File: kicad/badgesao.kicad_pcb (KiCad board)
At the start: 6 copper layers, 38.1 x 50.8 mm, 267 parts, among them J1 Conn_01x03_Pin, J2 DEBUG, J3 USB_C_Receptacle_USB2.0_16P, Q1 Q_NPN_BEC, SW1 SW_Push, SW2 SW_Push, SW3 SW_Push, SW4 SW_Push, SW5 SW_Push, SW6 SW_Push, SW7 SW_Push, SW8 SW_Push, U1 XC6206P332MR, U2 ZD25WQ32CEIGR, U3 LSM6DS3, U4 TPS61022, U6 RP2040, X1 Simple_Addon_v2, Y1 12M

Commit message: connected buzzer and sel nets
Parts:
- J1: value Conn_01x03_Pin -> DISP_DBG
- LS1: value CMT-5023S-SMT-TR -> BUZZER
- Q1: value Q_NPN_BEC -> NPN_BEC
- SW1: value SW_Push -> UP
- SW2: value SW_Push -> DOWN
- SW3: value SW_Push -> LEFT
- SW4: value SW_Push -> RIGHT
- SW5: value SW_Push -> B
- SW6: value SW_Push -> A
- SW7: value SW_Push -> RESET
- SW8: value SW_Push -> BOOTSEL
- U1: value XC6206P332MR -> 3V3LDO
- U2: value ZD25WQ32CEIGR -> 32Mb QSPI
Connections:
- U6 pad 37: unconnected-(U6-GPIO25-Pad37) -> /BUZZER
- U6 pad 41: unconnected-(U6-GPIO29_ADC3-Pad41) -> /BOOTSEL

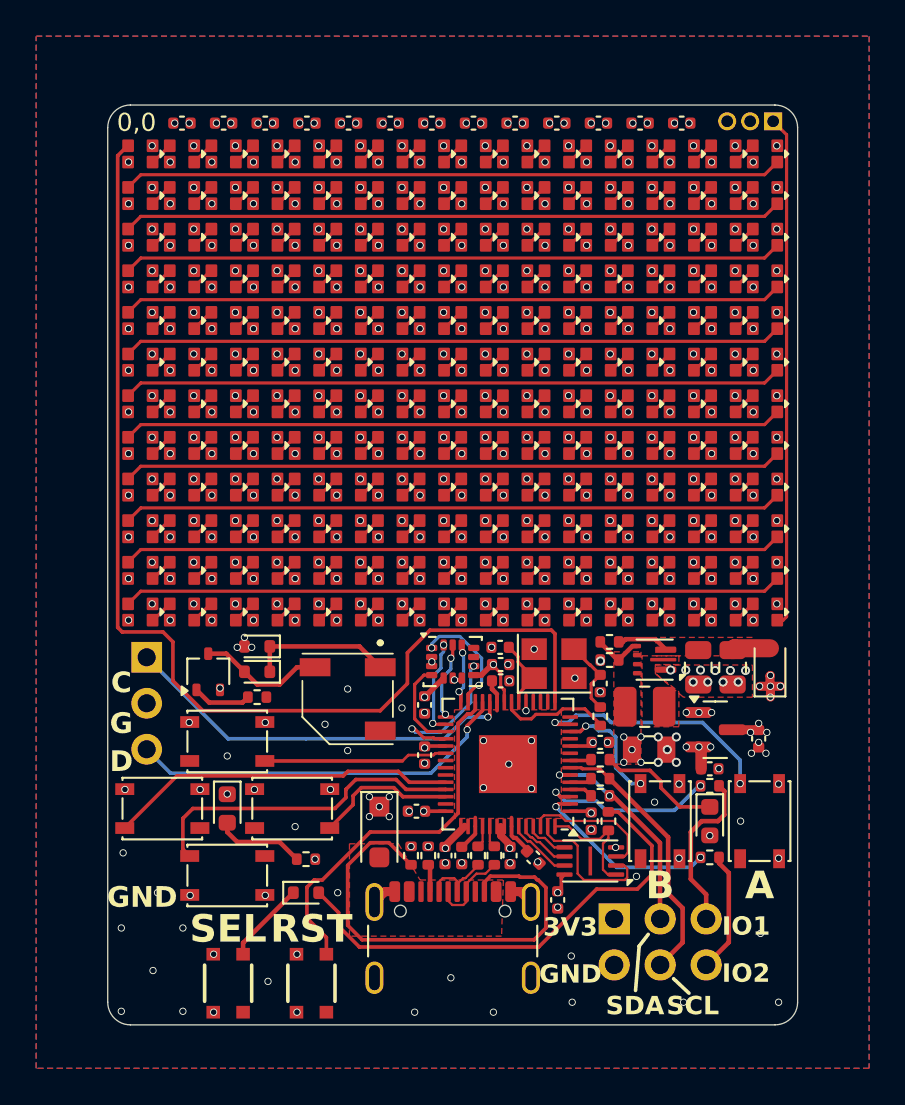
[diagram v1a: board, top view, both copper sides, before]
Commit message: fixed all rev0 issues
connected buzzer and bootsel nets
changed IMU to I2C mode
changed IMU to the cheaper -C model
changed all buttons to PTS815
changed order of WS2812s so that the frame buffer can be shifted monolithically
changed boost converter feedback network to use JLCPCB basic parts
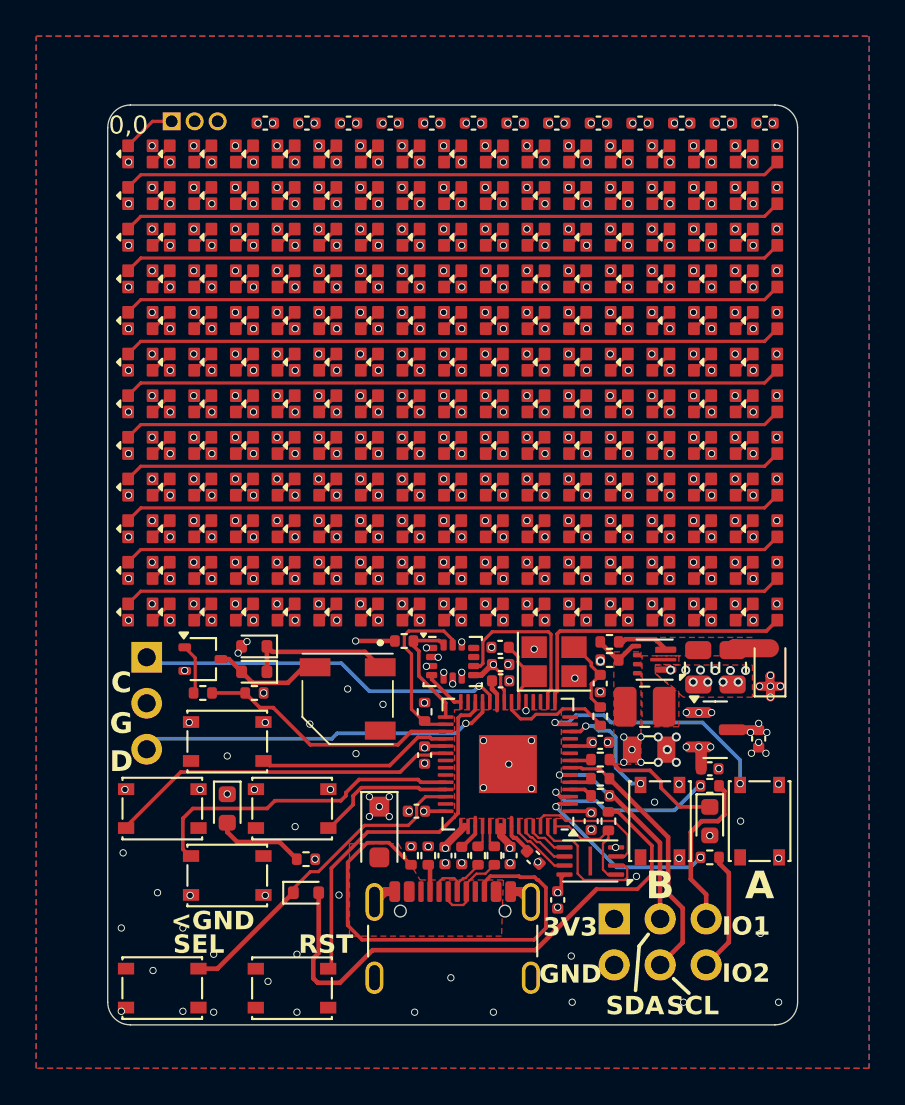
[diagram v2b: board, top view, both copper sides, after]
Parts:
- removed C14: 1u, Capacitor_SMD:C_0402_1005Metric
- added R16: 1k, Resistor_SMD:R_0402_1005Metric, F.Cu at (116.0, 83.3)
- added R17: 5k1, Resistor_SMD:R_0402_1005Metric, F.Cu at (124.3, 80.4)
- added R18: 5k1, Resistor_SMD:R_0402_1005Metric, F.Cu at (125.5, 84.3)
- R10, R8: value 27 -> 33
- R6: value 62k -> 200k
- R9: value 10k -> 33k
- SW7, SW8: footprint kmj_custom:PTS830GM140SMTRLFS -> kmj_custom:SW_SPST_PTS810
- U3: value LSM6DS3 -> LSM6DS3TR-C
- moved J1 33.2 mm to (111.5, 51.7), turned to -90 degrees
- moved C9 4.60 mm to (135.1, 51.8)
- moved C1 4.60 mm to (116.7, 51.8)
- moved C2 4.60 mm to (119.0, 51.8)
- moved C6 4.60 mm to (128.2, 51.8)
- moved C10 4.60 mm to (137.3, 51.8)
- moved C22 4.60 mm to (139.7, 51.8)
- moved C24 4.60 mm to (141.9, 51.8)
- moved C3 4.60 mm to (121.2, 51.8)
- moved C31 4.60 mm to (144.2, 51.8)
- moved C4 4.60 mm to (123.5, 51.8)
- moved C5 4.60 mm to (125.8, 51.8)
- moved C7 4.60 mm to (130.4, 51.8)
- moved C8 4.60 mm to (132.8, 51.8)
- moved SW8 3.65 mm to (111.0, 99.6), turned to 180 degrees
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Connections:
- D1 pad DIN: /WS2812_DIN -> Net-(D1-PadDIN)
- D1 pad DOUT: Net-(D1-PadDOUT) -> /Display/WS2812_LASTDOUT
- D101 pad DIN: Net-(D100-PadDOUT) -> Net-(D101-PadDIN)
- D101 pad DOUT: Net-(D101-PadDOUT) -> Net-(D100-PadDIN)
- D102 pad DIN: Net-(D101-PadDOUT) -> Net-(D102-PadDIN)
- D102 pad DOUT: Net-(D102-PadDOUT) -> Net-(D101-PadDIN)
- D103 pad DIN: Net-(D102-PadDOUT) -> Net-(D103-PadDIN)
- D103 pad DOUT: Net-(D103-PadDOUT) -> Net-(D102-PadDIN)
- D104 pad DIN: Net-(D103-PadDOUT) -> Net-(D104-PadDIN)
- D104 pad DOUT: Net-(D104-PadDOUT) -> Net-(D103-PadDIN)
- D105 pad DIN: Net-(D104-PadDOUT) -> Net-(D105-PadDIN)
- D105 pad DOUT: Net-(D105-PadDOUT) -> Net-(D104-PadDIN)
- D106 pad DIN: Net-(D105-PadDOUT) -> Net-(D106-PadDIN)
- D106 pad DOUT: Net-(D106-PadDOUT) -> Net-(D105-PadDIN)
- D107 pad DIN: Net-(D106-PadDOUT) -> Net-(D107-PadDIN)
- D107 pad DOUT: Net-(D107-PadDOUT) -> Net-(D106-PadDIN)
- D108 pad DIN: Net-(D107-PadDOUT) -> Net-(D108-PadDIN)
- D108 pad DOUT: Net-(D108-PadDOUT) -> Net-(D107-PadDIN)
- D109 pad DIN: Net-(D108-PadDOUT) -> Net-(D109-PadDIN)
- D109 pad DOUT: Net-(D109-PadDOUT) -> Net-(D108-PadDIN)
- D11 pad DIN: Net-(D10-PadDOUT) -> Net-(D11-PadDIN)
- D11 pad DOUT: Net-(D11-PadDOUT) -> Net-(D10-PadDIN)
- D110 pad DIN: Net-(D109-PadDOUT) -> Net-(D110-PadDIN)
- D110 pad DOUT: Net-(D110-PadDOUT) -> Net-(D109-PadDIN)
- D111 pad DIN: Net-(D110-PadDOUT) -> Net-(D111-PadDIN)
- D111 pad DOUT: Net-(D111-PadDOUT) -> Net-(D110-PadDIN)
- D112 pad DIN: Net-(D111-PadDOUT) -> Net-(D112-PadDIN)
- D112 pad DOUT: Net-(D112-PadDOUT) -> Net-(D111-PadDIN)
- D113 pad DIN: Net-(D112-PadDOUT) -> Net-(D113-PadDIN)
- D113 pad DOUT: Net-(D113-PadDOUT) -> Net-(D112-PadDIN)
- D114 pad DIN: Net-(D113-PadDOUT) -> Net-(D114-PadDIN)
- D114 pad DOUT: Net-(D114-PadDOUT) -> Net-(D113-PadDIN)
- D115 pad DIN: Net-(D114-PadDOUT) -> Net-(D115-PadDIN)
- D115 pad DOUT: Net-(D115-PadDOUT) -> Net-(D114-PadDIN)
- D116 pad DIN: Net-(D115-PadDOUT) -> Net-(D116-PadDIN)
- D116 pad DOUT: Net-(D116-PadDOUT) -> Net-(D115-PadDIN)
- D117 pad DIN: Net-(D116-PadDOUT) -> Net-(D117-PadDIN)
- D117 pad DOUT: Net-(D117-PadDOUT) -> Net-(D116-PadDIN)
- D118 pad DIN: Net-(D117-PadDOUT) -> Net-(D118-PadDIN)
- D118 pad DOUT: Net-(D118-PadDOUT) -> Net-(D117-PadDIN)
- D119 pad DIN: Net-(D118-PadDOUT) -> Net-(D119-PadDIN)
- D119 pad DOUT: Net-(D119-PadDOUT) -> Net-(D118-PadDIN)
- D12 pad DIN: Net-(D11-PadDOUT) -> Net-(D12-PadDIN)
- D12 pad DOUT: Net-(D12-PadDOUT) -> Net-(D11-PadDIN)
- D120 pad DIN: Net-(D119-PadDOUT) -> Net-(D120-PadDIN)
- D120 pad DOUT: Net-(D120-PadDOUT) -> Net-(D119-PadDIN)
- D121 pad DIN: Net-(D120-PadDOUT) -> Net-(D121-PadDIN)
- D121 pad DOUT: Net-(D121-PadDOUT) -> Net-(D120-PadDIN)
- D122 pad DIN: Net-(D121-PadDOUT) -> Net-(D122-PadDIN)
- D122 pad DOUT: Net-(D122-PadDOUT) -> Net-(D121-PadDIN)
- D123 pad DIN: Net-(D122-PadDOUT) -> Net-(D123-PadDIN)
- D123 pad DOUT: Net-(D123-PadDOUT) -> Net-(D122-PadDIN)
- D124 pad DIN: Net-(D123-PadDOUT) -> Net-(D124-PadDIN)
- D124 pad DOUT: Net-(D124-PadDOUT) -> Net-(D123-PadDIN)
- D125 pad DIN: Net-(D124-PadDOUT) -> Net-(D125-PadDIN)
- D125 pad DOUT: Net-(D125-PadDOUT) -> Net-(D124-PadDIN)
- D126 pad DIN: Net-(D125-PadDOUT) -> Net-(D126-PadDIN)
- D126 pad DOUT: Net-(D126-PadDOUT) -> Net-(D125-PadDIN)
- D127 pad DIN: Net-(D126-PadDOUT) -> Net-(D127-PadDIN)
- D127 pad DOUT: Net-(D127-PadDOUT) -> Net-(D126-PadDIN)
- D128 pad DIN: Net-(D127-PadDOUT) -> Net-(D128-PadDIN)
- D128 pad DOUT: Net-(D128-PadDOUT) -> Net-(D127-PadDIN)
- D129 pad DIN: Net-(D128-PadDOUT) -> Net-(D129-PadDIN)
- D129 pad DOUT: Net-(D129-PadDOUT) -> Net-(D128-PadDIN)
- D13 pad DIN: Net-(D12-PadDOUT) -> Net-(D13-PadDIN)
- D13 pad DOUT: Net-(D13-PadDOUT) -> Net-(D12-PadDIN)
- D130 pad DIN: Net-(D129-PadDOUT) -> Net-(D130-PadDIN)
- D130 pad DOUT: Net-(D130-PadDOUT) -> Net-(D129-PadDIN)
- D131 pad DIN: Net-(D130-PadDOUT) -> Net-(D131-PadDIN)
- D131 pad DOUT: Net-(D131-PadDOUT) -> Net-(D130-PadDIN)
- D132 pad DIN: Net-(D131-PadDOUT) -> Net-(D132-PadDIN)
- D132 pad DOUT: Net-(D132-PadDOUT) -> Net-(D131-PadDIN)
- D133 pad DIN: Net-(D132-PadDOUT) -> Net-(D133-PadDIN)
- D133 pad DOUT: Net-(D133-PadDOUT) -> Net-(D132-PadDIN)
- D134 pad DIN: Net-(D133-PadDOUT) -> Net-(D134-PadDIN)
- D134 pad DOUT: Net-(D134-PadDOUT) -> Net-(D133-PadDIN)
- D135 pad DIN: Net-(D134-PadDOUT) -> Net-(D135-PadDIN)
- D135 pad DOUT: Net-(D135-PadDOUT) -> Net-(D134-PadDIN)
- D136 pad DIN: Net-(D135-PadDOUT) -> Net-(D136-PadDIN)
- D136 pad DOUT: Net-(D136-PadDOUT) -> Net-(D135-PadDIN)
- D137 pad DIN: Net-(D136-PadDOUT) -> Net-(D137-PadDIN)
- D137 pad DOUT: Net-(D137-PadDOUT) -> Net-(D136-PadDIN)
- D138 pad DIN: Net-(D137-PadDOUT) -> Net-(D138-PadDIN)
- D138 pad DOUT: Net-(D138-PadDOUT) -> Net-(D137-PadDIN)
- D139 pad DIN: Net-(D138-PadDOUT) -> Net-(D139-PadDIN)
- D139 pad DOUT: Net-(D139-PadDOUT) -> Net-(D138-PadDIN)
- D14 pad DIN: Net-(D13-PadDOUT) -> Net-(D14-PadDIN)
- D14 pad DOUT: Net-(D14-PadDOUT) -> Net-(D13-PadDIN)
- D140 pad DIN: Net-(D139-PadDOUT) -> Net-(D140-PadDIN)
- D140 pad DOUT: Net-(D140-PadDOUT) -> Net-(D139-PadDIN)
- D141 pad DIN: Net-(D140-PadDOUT) -> Net-(D141-PadDIN)
- D141 pad DOUT: Net-(D141-PadDOUT) -> Net-(D140-PadDIN)
- D142 pad DIN: Net-(D141-PadDOUT) -> Net-(D142-PadDIN)
- D142 pad DOUT: Net-(D142-PadDOUT) -> Net-(D141-PadDIN)
- D143 pad DIN: Net-(D142-PadDOUT) -> Net-(D143-PadDIN)
- D143 pad DOUT: Net-(D143-PadDOUT) -> Net-(D142-PadDIN)
- D144 pad DIN: Net-(D143-PadDOUT) -> Net-(D144-PadDIN)
- D144 pad DOUT: Net-(D144-PadDOUT) -> Net-(D143-PadDIN)
- D145 pad DIN: Net-(D144-PadDOUT) -> Net-(D145-PadDIN)
- D145 pad DOUT: Net-(D145-PadDOUT) -> Net-(D144-PadDIN)
- D146 pad DIN: Net-(D145-PadDOUT) -> Net-(D146-PadDIN)
- D146 pad DOUT: Net-(D146-PadDOUT) -> Net-(D145-PadDIN)
- D147 pad DIN: Net-(D146-PadDOUT) -> Net-(D147-PadDIN)
- D147 pad DOUT: Net-(D147-PadDOUT) -> Net-(D146-PadDIN)
- D148 pad DIN: Net-(D147-PadDOUT) -> Net-(D148-PadDIN)
- D148 pad DOUT: Net-(D148-PadDOUT) -> Net-(D147-PadDIN)
- D149 pad DIN: Net-(D148-PadDOUT) -> Net-(D149-PadDIN)
- D149 pad DOUT: Net-(D149-PadDOUT) -> Net-(D148-PadDIN)
- D15 pad DIN: Net-(D14-PadDOUT) -> Net-(D15-PadDIN)
- D15 pad DOUT: Net-(D15-PadDOUT) -> Net-(D14-PadDIN)
- D150 pad DIN: Net-(D149-PadDOUT) -> Net-(D150-PadDIN)
- D150 pad DOUT: Net-(D150-PadDOUT) -> Net-(D149-PadDIN)
- D151 pad DIN: Net-(D150-PadDOUT) -> Net-(D151-PadDIN)
- D151 pad DOUT: Net-(D151-PadDOUT) -> Net-(D150-PadDIN)
- D152 pad DIN: Net-(D151-PadDOUT) -> Net-(D152-PadDIN)
- D152 pad DOUT: Net-(D152-PadDOUT) -> Net-(D151-PadDIN)
- D153 pad DIN: Net-(D152-PadDOUT) -> Net-(D153-PadDIN)
- D153 pad DOUT: Net-(D153-PadDOUT) -> Net-(D152-PadDIN)
- D154 pad DIN: Net-(D153-PadDOUT) -> Net-(D154-PadDIN)
- D154 pad DOUT: Net-(D154-PadDOUT) -> Net-(D153-PadDIN)
- D155 pad DIN: Net-(D154-PadDOUT) -> Net-(D155-PadDIN)
- D155 pad DOUT: Net-(D155-PadDOUT) -> Net-(D154-PadDIN)
- D156 pad DIN: Net-(D155-PadDOUT) -> Net-(D156-PadDIN)
- D156 pad DOUT: Net-(D156-PadDOUT) -> Net-(D155-PadDIN)
- D157 pad DIN: Net-(D156-PadDOUT) -> Net-(D157-PadDIN)
- D157 pad DOUT: Net-(D157-PadDOUT) -> Net-(D156-PadDIN)
- D158 pad DIN: Net-(D157-PadDOUT) -> Net-(D158-PadDIN)
- D158 pad DOUT: Net-(D158-PadDOUT) -> Net-(D157-PadDIN)
- D159 pad DIN: Net-(D158-PadDOUT) -> Net-(D159-PadDIN)
- D159 pad DOUT: Net-(D159-PadDOUT) -> Net-(D158-PadDIN)
- D16 pad DIN: Net-(D15-PadDOUT) -> Net-(D16-PadDIN)
- D16 pad DOUT: Net-(D16-PadDOUT) -> Net-(D15-PadDIN)
- D160 pad DIN: Net-(D159-PadDOUT) -> Net-(D160-PadDIN)
- D160 pad DOUT: Net-(D160-PadDOUT) -> Net-(D159-PadDIN)
- D161 pad DIN: Net-(D160-PadDOUT) -> Net-(D161-PadDIN)
- D161 pad DOUT: Net-(D161-PadDOUT) -> Net-(D160-PadDIN)
- D162 pad DIN: Net-(D161-PadDOUT) -> Net-(D162-PadDIN)
- D162 pad DOUT: Net-(D162-PadDOUT) -> Net-(D161-PadDIN)
- D163 pad DIN: Net-(D162-PadDOUT) -> Net-(D163-PadDIN)
- D163 pad DOUT: Net-(D163-PadDOUT) -> Net-(D162-PadDIN)
- D164 pad DIN: Net-(D163-PadDOUT) -> Net-(D164-PadDIN)
- D164 pad DOUT: Net-(D164-PadDOUT) -> Net-(D163-PadDIN)
- D165 pad DIN: Net-(D164-PadDOUT) -> Net-(D165-PadDIN)
- D165 pad DOUT: Net-(D165-PadDOUT) -> Net-(D164-PadDIN)
- D166 pad DIN: Net-(D165-PadDOUT) -> Net-(D166-PadDIN)
- D166 pad DOUT: Net-(D166-PadDOUT) -> Net-(D165-PadDIN)
- D167 pad DIN: Net-(D166-PadDOUT) -> Net-(D167-PadDIN)
- D167 pad DOUT: Net-(D167-PadDOUT) -> Net-(D166-PadDIN)
- D168 pad DIN: Net-(D167-PadDOUT) -> Net-(D168-PadDIN)
- D168 pad DOUT: Net-(D168-PadDOUT) -> Net-(D167-PadDIN)
- D169 pad DIN: Net-(D168-PadDOUT) -> Net-(D169-PadDIN)
- D169 pad DOUT: Net-(D169-PadDOUT) -> Net-(D168-PadDIN)
- D17 pad DIN: Net-(D16-PadDOUT) -> Net-(D17-PadDIN)
- D17 pad DOUT: Net-(D17-PadDOUT) -> Net-(D16-PadDIN)
- D170 pad DIN: Net-(D169-PadDOUT) -> Net-(D170-PadDIN)
- D170 pad DOUT: Net-(D170-PadDOUT) -> Net-(D169-PadDIN)
- D171 pad DIN: Net-(D170-PadDOUT) -> Net-(D171-PadDIN)
- D171 pad DOUT: Net-(D171-PadDOUT) -> Net-(D170-PadDIN)
- D172 pad DIN: Net-(D171-PadDOUT) -> Net-(D172-PadDIN)
- D172 pad DOUT: Net-(D172-PadDOUT) -> Net-(D171-PadDIN)
- D173 pad DIN: Net-(D172-PadDOUT) -> Net-(D173-PadDIN)
- D173 pad DOUT: Net-(D173-PadDOUT) -> Net-(D172-PadDIN)
- D174 pad DIN: Net-(D173-PadDOUT) -> Net-(D174-PadDIN)
- D174 pad DOUT: Net-(D174-PadDOUT) -> Net-(D173-PadDIN)
- D175 pad DIN: Net-(D174-PadDOUT) -> Net-(D175-PadDIN)
- D175 pad DOUT: Net-(D175-PadDOUT) -> Net-(D174-PadDIN)
- D176 pad DIN: Net-(D175-PadDOUT) -> Net-(D176-PadDIN)
- D176 pad DOUT: Net-(D176-PadDOUT) -> Net-(D175-PadDIN)
- D177 pad DIN: Net-(D176-PadDOUT) -> Net-(D177-PadDIN)
- D177 pad DOUT: Net-(D177-PadDOUT) -> Net-(D176-PadDIN)
- D178 pad DIN: Net-(D177-PadDOUT) -> Net-(D178-PadDIN)
- D178 pad DOUT: Net-(D178-PadDOUT) -> Net-(D177-PadDIN)
- D179 pad DIN: Net-(D178-PadDOUT) -> Net-(D179-PadDIN)
- D179 pad DOUT: Net-(D179-PadDOUT) -> Net-(D178-PadDIN)
- D18 pad DIN: Net-(D17-PadDOUT) -> Net-(D18-PadDIN)
- D18 pad DOUT: Net-(D18-PadDOUT) -> Net-(D17-PadDIN)
- D180 pad DIN: Net-(D179-PadDOUT) -> Net-(D180-PadDIN)
- D180 pad DOUT: Net-(D180-PadDOUT) -> Net-(D179-PadDIN)
- D181 pad DIN: Net-(D180-PadDOUT) -> Net-(D181-PadDIN)
- D181 pad DOUT: Net-(D181-PadDOUT) -> Net-(D180-PadDIN)
- D182 pad DIN: Net-(D181-PadDOUT) -> Net-(D182-PadDIN)
- D182 pad DOUT: Net-(D182-PadDOUT) -> Net-(D181-PadDIN)
- D183 pad DIN: Net-(D182-PadDOUT) -> Net-(D183-PadDIN)
- D183 pad DOUT: Net-(D183-PadDOUT) -> Net-(D182-PadDIN)
- D184 pad DIN: Net-(D183-PadDOUT) -> Net-(D184-PadDIN)
- D184 pad DOUT: Net-(D184-PadDOUT) -> Net-(D183-PadDIN)
- D185 pad DIN: Net-(D184-PadDOUT) -> Net-(D185-PadDIN)
- D185 pad DOUT: Net-(D185-PadDOUT) -> Net-(D184-PadDIN)
- D186 pad DIN: Net-(D185-PadDOUT) -> Net-(D186-PadDIN)
- D186 pad DOUT: Net-(D186-PadDOUT) -> Net-(D185-PadDIN)
- D187 pad DIN: Net-(D186-PadDOUT) -> Net-(D187-PadDIN)
- D187 pad DOUT: Net-(D187-PadDOUT) -> Net-(D186-PadDIN)
- D188 pad DIN: Net-(D187-PadDOUT) -> Net-(D188-PadDIN)
- D188 pad DOUT: Net-(D188-PadDOUT) -> Net-(D187-PadDIN)
- D189 pad DIN: Net-(D188-PadDOUT) -> Net-(D189-PadDIN)
- D189 pad DOUT: Net-(D189-PadDOUT) -> Net-(D188-PadDIN)
- D19 pad DIN: Net-(D18-PadDOUT) -> Net-(D19-PadDIN)
- D19 pad DOUT: Net-(D19-PadDOUT) -> Net-(D18-PadDIN)
- D190 pad DIN: Net-(D189-PadDOUT) -> Net-(D190-PadDIN)
- D190 pad DOUT: Net-(D190-PadDOUT) -> Net-(D189-PadDIN)
- D191 pad DIN: Net-(D190-PadDOUT) -> Net-(D191-PadDIN)
- D191 pad DOUT: Net-(D191-PadDOUT) -> Net-(D190-PadDIN)
- D192 pad DIN: Net-(D191-PadDOUT) -> /WS2812_DIN
- D192 pad DOUT: /Display/WS2812_LASTDOUT -> Net-(D191-PadDIN)
- D2 pad DIN: Net-(D1-PadDOUT) -> Net-(D2-PadDIN)
- D2 pad DOUT: Net-(D2-PadDOUT) -> Net-(D1-PadDIN)
- D20 pad DIN: Net-(D19-PadDOUT) -> Net-(D20-PadDIN)
- D20 pad DOUT: Net-(D20-PadDOUT) -> Net-(D19-PadDIN)
- D21 pad DIN: Net-(D20-PadDOUT) -> Net-(D21-PadDIN)
- D21 pad DOUT: Net-(D21-PadDOUT) -> Net-(D20-PadDIN)
- D22 pad DIN: Net-(D21-PadDOUT) -> Net-(D22-PadDIN)
- D22 pad DOUT: Net-(D22-PadDOUT) -> Net-(D21-PadDIN)
- D23 pad DIN: Net-(D22-PadDOUT) -> Net-(D23-PadDIN)
- D23 pad DOUT: Net-(D23-PadDOUT) -> Net-(D22-PadDIN)
- D24 pad DIN: Net-(D23-PadDOUT) -> Net-(D24-PadDIN)
- D24 pad DOUT: Net-(D24-PadDOUT) -> Net-(D23-PadDIN)
- D25 pad DIN: Net-(D24-PadDOUT) -> Net-(D25-PadDIN)
- D25 pad DOUT: Net-(D25-PadDOUT) -> Net-(D24-PadDIN)
- D26 pad DIN: Net-(D25-PadDOUT) -> Net-(D26-PadDIN)
- D26 pad DOUT: Net-(D26-PadDOUT) -> Net-(D25-PadDIN)
- D27 pad DIN: Net-(D26-PadDOUT) -> Net-(D27-PadDIN)
- D27 pad DOUT: Net-(D27-PadDOUT) -> Net-(D26-PadDIN)
- D28 pad DIN: Net-(D27-PadDOUT) -> Net-(D28-PadDIN)
- D28 pad DOUT: Net-(D28-PadDOUT) -> Net-(D27-PadDIN)
- D29 pad DIN: Net-(D28-PadDOUT) -> Net-(D29-PadDIN)
- D29 pad DOUT: Net-(D29-PadDOUT) -> Net-(D28-PadDIN)
- D3 pad DIN: Net-(D2-PadDOUT) -> Net-(D3-PadDIN)
- D3 pad DOUT: Net-(D3-PadDOUT) -> Net-(D2-PadDIN)
- D30 pad DIN: Net-(D29-PadDOUT) -> Net-(D30-PadDIN)
- D30 pad DOUT: Net-(D30-PadDOUT) -> Net-(D29-PadDIN)
- D31 pad DIN: Net-(D30-PadDOUT) -> Net-(D31-PadDIN)
- D31 pad DOUT: Net-(D31-PadDOUT) -> Net-(D30-PadDIN)
- D32 pad DIN: Net-(D31-PadDOUT) -> Net-(D32-PadDIN)
- D32 pad DOUT: Net-(D32-PadDOUT) -> Net-(D31-PadDIN)
- D33 pad DIN: Net-(D32-PadDOUT) -> Net-(D33-PadDIN)
- D33 pad DOUT: Net-(D33-PadDOUT) -> Net-(D32-PadDIN)
- D34 pad DIN: Net-(D33-PadDOUT) -> Net-(D34-PadDIN)
- D34 pad DOUT: Net-(D34-PadDOUT) -> Net-(D33-PadDIN)
- D35 pad DIN: Net-(D34-PadDOUT) -> Net-(D35-PadDIN)
- D35 pad DOUT: Net-(D35-PadDOUT) -> Net-(D34-PadDIN)
- D36 pad DIN: Net-(D35-PadDOUT) -> Net-(D36-PadDIN)
- D36 pad DOUT: Net-(D36-PadDOUT) -> Net-(D35-PadDIN)
- D37 pad DIN: Net-(D36-PadDOUT) -> Net-(D37-PadDIN)
- D37 pad DOUT: Net-(D37-PadDOUT) -> Net-(D36-PadDIN)
- D38 pad DIN: Net-(D37-PadDOUT) -> Net-(D38-PadDIN)
- D38 pad DOUT: Net-(D38-PadDOUT) -> Net-(D37-PadDIN)
- D39 pad DIN: Net-(D38-PadDOUT) -> Net-(D39-PadDIN)
- D39 pad DOUT: Net-(D39-PadDOUT) -> Net-(D38-PadDIN)
- D4 pad DIN: Net-(D3-PadDOUT) -> Net-(D4-PadDIN)
- D4 pad DOUT: Net-(D4-PadDOUT) -> Net-(D3-PadDIN)
- D40 pad DIN: Net-(D39-PadDOUT) -> Net-(D40-PadDIN)
- D40 pad DOUT: Net-(D40-PadDOUT) -> Net-(D39-PadDIN)
- D41 pad DIN: Net-(D40-PadDOUT) -> Net-(D41-PadDIN)
- D41 pad DOUT: Net-(D41-PadDOUT) -> Net-(D40-PadDIN)
- D42 pad DIN: Net-(D41-PadDOUT) -> Net-(D42-PadDIN)
- D42 pad DOUT: Net-(D42-PadDOUT) -> Net-(D41-PadDIN)
- D43 pad DIN: Net-(D42-PadDOUT) -> Net-(D43-PadDIN)
- D43 pad DOUT: Net-(D43-PadDOUT) -> Net-(D42-PadDIN)
- D44 pad DIN: Net-(D43-PadDOUT) -> Net-(D44-PadDIN)
- D44 pad DOUT: Net-(D44-PadDOUT) -> Net-(D43-PadDIN)
- D45 pad DIN: Net-(D44-PadDOUT) -> Net-(D45-PadDIN)
- D45 pad DOUT: Net-(D45-PadDOUT) -> Net-(D44-PadDIN)
- D46 pad DIN: Net-(D45-PadDOUT) -> Net-(D46-PadDIN)
- D46 pad DOUT: Net-(D46-PadDOUT) -> Net-(D45-PadDIN)
- D47 pad DIN: Net-(D46-PadDOUT) -> Net-(D47-PadDIN)
- D47 pad DOUT: Net-(D47-PadDOUT) -> Net-(D46-PadDIN)
- D48 pad DIN: Net-(D47-PadDOUT) -> Net-(D48-PadDIN)
- D48 pad DOUT: Net-(D48-PadDOUT) -> Net-(D47-PadDIN)
- D49 pad DIN: Net-(D48-PadDOUT) -> Net-(D49-PadDIN)
- D49 pad DOUT: Net-(D49-PadDOUT) -> Net-(D48-PadDIN)
- D5 pad DIN: Net-(D4-PadDOUT) -> Net-(D5-PadDIN)
- D5 pad DOUT: Net-(D5-PadDOUT) -> Net-(D4-PadDIN)
- D50 pad DIN: Net-(D49-PadDOUT) -> Net-(D50-PadDIN)
- D50 pad DOUT: Net-(D50-PadDOUT) -> Net-(D49-PadDIN)
- D51 pad DIN: Net-(D50-PadDOUT) -> Net-(D51-PadDIN)
- D51 pad DOUT: Net-(D51-PadDOUT) -> Net-(D50-PadDIN)
- D52 pad DIN: Net-(D51-PadDOUT) -> Net-(D52-PadDIN)
- D52 pad DOUT: Net-(D52-PadDOUT) -> Net-(D51-PadDIN)
- D53 pad DIN: Net-(D52-PadDOUT) -> Net-(D53-PadDIN)
- D53 pad DOUT: Net-(D53-PadDOUT) -> Net-(D52-PadDIN)
- D54 pad DIN: Net-(D53-PadDOUT) -> Net-(D54-PadDIN)
- D54 pad DOUT: Net-(D54-PadDOUT) -> Net-(D53-PadDIN)
- D55 pad DIN: Net-(D54-PadDOUT) -> Net-(D55-PadDIN)
- D55 pad DOUT: Net-(D55-PadDOUT) -> Net-(D54-PadDIN)
- D56 pad DIN: Net-(D55-PadDOUT) -> Net-(D56-PadDIN)
- D56 pad DOUT: Net-(D56-PadDOUT) -> Net-(D55-PadDIN)
- D57 pad DIN: Net-(D56-PadDOUT) -> Net-(D57-PadDIN)
- D57 pad DOUT: Net-(D57-PadDOUT) -> Net-(D56-PadDIN)
- D58 pad DIN: Net-(D57-PadDOUT) -> Net-(D58-PadDIN)
- D58 pad DOUT: Net-(D58-PadDOUT) -> Net-(D57-PadDIN)
- D59 pad DIN: Net-(D58-PadDOUT) -> Net-(D59-PadDIN)
- D59 pad DOUT: Net-(D59-PadDOUT) -> Net-(D58-PadDIN)
- D6 pad DIN: Net-(D5-PadDOUT) -> Net-(D6-PadDIN)
- D6 pad DOUT: Net-(D6-PadDOUT) -> Net-(D5-PadDIN)
- D60 pad DIN: Net-(D59-PadDOUT) -> Net-(D60-PadDIN)
- D60 pad DOUT: Net-(D60-PadDOUT) -> Net-(D59-PadDIN)
- D61 pad DIN: Net-(D60-PadDOUT) -> Net-(D61-PadDIN)
- D61 pad DOUT: Net-(D61-PadDOUT) -> Net-(D60-PadDIN)
- D62 pad DIN: Net-(D61-PadDOUT) -> Net-(D62-PadDIN)
- D62 pad DOUT: Net-(D62-PadDOUT) -> Net-(D61-PadDIN)
- D63 pad DIN: Net-(D62-PadDOUT) -> Net-(D63-PadDIN)
- D63 pad DOUT: Net-(D63-PadDOUT) -> Net-(D62-PadDIN)
- D64 pad DIN: Net-(D63-PadDOUT) -> Net-(D64-PadDIN)
- D64 pad DOUT: Net-(D64-PadDOUT) -> Net-(D63-PadDIN)
- D65 pad DIN: Net-(D64-PadDOUT) -> Net-(D65-PadDIN)
- D65 pad DOUT: Net-(D65-PadDOUT) -> Net-(D64-PadDIN)
- D66 pad DIN: Net-(D65-PadDOUT) -> Net-(D66-PadDIN)
- D66 pad DOUT: Net-(D66-PadDOUT) -> Net-(D65-PadDIN)
- D67 pad DIN: Net-(D66-PadDOUT) -> Net-(D67-PadDIN)
- D67 pad DOUT: Net-(D67-PadDOUT) -> Net-(D66-PadDIN)
- D68 pad DIN: Net-(D67-PadDOUT) -> Net-(D68-PadDIN)
- D68 pad DOUT: Net-(D68-PadDOUT) -> Net-(D67-PadDIN)
- D69 pad DIN: Net-(D68-PadDOUT) -> Net-(D69-PadDIN)
- D69 pad DOUT: Net-(D69-PadDOUT) -> Net-(D68-PadDIN)
- D7 pad DIN: Net-(D6-PadDOUT) -> Net-(D7-PadDIN)
- D7 pad DOUT: Net-(D7-PadDOUT) -> Net-(D6-PadDIN)
- D70 pad DIN: Net-(D69-PadDOUT) -> Net-(D70-PadDIN)
- D70 pad DOUT: Net-(D70-PadDOUT) -> Net-(D69-PadDIN)
- D71 pad DIN: Net-(D70-PadDOUT) -> Net-(D71-PadDIN)
- D71 pad DOUT: Net-(D71-PadDOUT) -> Net-(D70-PadDIN)
- D72 pad DIN: Net-(D71-PadDOUT) -> Net-(D72-PadDIN)
- D72 pad DOUT: Net-(D72-PadDOUT) -> Net-(D71-PadDIN)
- D73 pad DIN: Net-(D72-PadDOUT) -> Net-(D73-PadDIN)
- D73 pad DOUT: Net-(D73-PadDOUT) -> Net-(D72-PadDIN)
- D74 pad DIN: Net-(D73-PadDOUT) -> Net-(D74-PadDIN)
- D74 pad DOUT: Net-(D74-PadDOUT) -> Net-(D73-PadDIN)
- D75 pad DIN: Net-(D74-PadDOUT) -> Net-(D75-PadDIN)
- D75 pad DOUT: Net-(D75-PadDOUT) -> Net-(D74-PadDIN)
- D76 pad DIN: Net-(D75-PadDOUT) -> Net-(D76-PadDIN)
- D76 pad DOUT: Net-(D76-PadDOUT) -> Net-(D75-PadDIN)
- D77 pad DIN: Net-(D76-PadDOUT) -> Net-(D77-PadDIN)
- D77 pad DOUT: Net-(D77-PadDOUT) -> Net-(D76-PadDIN)
- D78 pad DIN: Net-(D77-PadDOUT) -> Net-(D78-PadDIN)
- D78 pad DOUT: Net-(D78-PadDOUT) -> Net-(D77-PadDIN)
- D79 pad DIN: Net-(D78-PadDOUT) -> Net-(D79-PadDIN)
- D79 pad DOUT: Net-(D79-PadDOUT) -> Net-(D78-PadDIN)
- D8 pad DIN: Net-(D7-PadDOUT) -> Net-(D8-PadDIN)
- D8 pad DOUT: Net-(D8-PadDOUT) -> Net-(D7-PadDIN)
- D80 pad DIN: Net-(D79-PadDOUT) -> Net-(D80-PadDIN)
- D80 pad DOUT: Net-(D80-PadDOUT) -> Net-(D79-PadDIN)
- D81 pad DIN: Net-(D80-PadDOUT) -> Net-(D81-PadDIN)
- D81 pad DOUT: Net-(D81-PadDOUT) -> Net-(D80-PadDIN)
- D82 pad DIN: Net-(D81-PadDOUT) -> Net-(D82-PadDIN)
- D82 pad DOUT: Net-(D82-PadDOUT) -> Net-(D81-PadDIN)
- D83 pad DIN: Net-(D82-PadDOUT) -> Net-(D83-PadDIN)
- D83 pad DOUT: Net-(D83-PadDOUT) -> Net-(D82-PadDIN)
- D84 pad DIN: Net-(D83-PadDOUT) -> Net-(D84-PadDIN)
- D84 pad DOUT: Net-(D84-PadDOUT) -> Net-(D83-PadDIN)
- D85 pad DIN: Net-(D84-PadDOUT) -> Net-(D85-PadDIN)
- D85 pad DOUT: Net-(D85-PadDOUT) -> Net-(D84-PadDIN)
- D86 pad DIN: Net-(D85-PadDOUT) -> Net-(D86-PadDIN)
- D86 pad DOUT: Net-(D86-PadDOUT) -> Net-(D85-PadDIN)
- D87 pad DIN: Net-(D86-PadDOUT) -> Net-(D87-PadDIN)
- D87 pad DOUT: Net-(D87-PadDOUT) -> Net-(D86-PadDIN)
- D88 pad DIN: Net-(D87-PadDOUT) -> Net-(D88-PadDIN)
- D88 pad DOUT: Net-(D88-PadDOUT) -> Net-(D87-PadDIN)
- D89 pad DIN: Net-(D88-PadDOUT) -> Net-(D89-PadDIN)
- D89 pad DOUT: Net-(D89-PadDOUT) -> Net-(D88-PadDIN)
- D9 pad DIN: Net-(D8-PadDOUT) -> Net-(D10-PadDOUT)
- D9 pad DOUT: Net-(D10-PadDIN) -> Net-(D8-PadDIN)
- D90 pad DIN: Net-(D89-PadDOUT) -> Net-(D90-PadDIN)
- D90 pad DOUT: Net-(D90-PadDOUT) -> Net-(D89-PadDIN)
- D91 pad DIN: Net-(D90-PadDOUT) -> Net-(D91-PadDIN)
- D91 pad DOUT: Net-(D91-PadDOUT) -> Net-(D90-PadDIN)
- D92 pad DIN: Net-(D91-PadDOUT) -> Net-(D92-PadDIN)
- D92 pad DOUT: Net-(D92-PadDOUT) -> Net-(D91-PadDIN)
- D93 pad DIN: Net-(D92-PadDOUT) -> Net-(D93-PadDIN)
- D93 pad DOUT: Net-(D93-PadDOUT) -> Net-(D92-PadDIN)
- D94 pad DIN: Net-(D93-PadDOUT) -> Net-(D94-PadDIN)
- D94 pad DOUT: Net-(D94-PadDOUT) -> Net-(D93-PadDIN)
- D95 pad DIN: Net-(D94-PadDOUT) -> Net-(D95-PadDIN)
- D95 pad DOUT: Net-(D95-PadDOUT) -> Net-(D94-PadDIN)
- D96 pad DIN: Net-(D95-PadDOUT) -> Net-(D96-PadDIN)
- D96 pad DOUT: Net-(D96-PadDOUT) -> Net-(D95-PadDIN)
- D97 pad DIN: Net-(D96-PadDOUT) -> Net-(D97-PadDIN)
- D97 pad DOUT: Net-(D97-PadDOUT) -> Net-(D96-PadDIN)
- D98 pad DIN: Net-(D97-PadDOUT) -> Net-(D98-PadDIN)
- D98 pad DOUT: Net-(D98-PadDOUT) -> Net-(D97-PadDIN)
- D99 pad DIN: Net-(D98-PadDOUT) -> Net-(D100-PadDOUT)
- D99 pad DOUT: Net-(D100-PadDIN) -> Net-(D98-PadDIN)
- U3 pad 1: /SPI0_RX -> GND
- U3 pad 12: /SPI0_CSn -> +3V3
- U3 pad 13: /SPI0_SCK -> /I2C1_SCL
- U3 pad 14: /SPI0_TX -> /I2C1_SDA
- U3 pad 4: /SPI0_INT1 -> /IMU_INT1
- U3 pad 9: /SPI0_INT2 -> /IMU_INT2
- U6 pad 16: unconnected-(U6-GPIO13-Pad16) -> /IMU_INT2
- U6 pad 27: /SPI0_RX -> unconnected-(U6-GPIO16-Pad27)
- U6 pad 28: /SPI0_CSn -> /IMU_INT1
- U6 pad 29: /SPI0_SCK -> /I2C1_SDA
- U6 pad 30: /SPI0_TX -> /I2C1_SCL
- U6 pad 31: /SPI0_INT1 -> /BUZZER
- U6 pad 32: /SPI0_INT2 -> /UP
- U6 pad 34: /UP -> /LEFT
- U6 pad 37: /BUZZER -> unconnected-(U6-GPIO25-Pad37)
- U6 pad 38: /LEFT -> /DOWN
- U6 pad 39: /DOWN -> /RIGHT
- U6 pad 40: /RIGHT -> /BOOTSEL
- U6 pad 41: /BOOTSEL -> unconnected-(U6-GPIO29_ADC3-Pad41)
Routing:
- net /WS2812_DIN: track 60.8 -> 16.3 mm
- net Net-(D64-PadDOUT): track 36.4 -> 0.00 mm
- net Net-(D64-PadDIN): track 0.00 -> 36.4 mm
- net Net-(D48-PadDOUT): track 36.4 -> 0.00 mm
- net Net-(D48-PadDIN): track 0.00 -> 36.4 mm
- net Net-(D16-PadDOUT): track 36.4 -> 0.00 mm
- net Net-(D16-PadDIN): track 0.00 -> 36.4 mm
- net Net-(D144-PadDOUT): track 36.4 -> 0.00 mm
- net Net-(D144-PadDIN): track 0.00 -> 36.4 mm
- net Net-(D128-PadDOUT): track 36.4 -> 0.00 mm
- net Net-(D128-PadDIN): track 0.00 -> 36.4 mm
- net Net-(D112-PadDOUT): track 36.4 -> 0.00 mm
- net Net-(D112-PadDIN): track 0.00 -> 36.4 mm
- net Net-(D80-PadDOUT): track 36.4 -> 0.00 mm
- net Net-(D80-PadDIN): track 0.00 -> 36.4 mm
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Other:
- board text added: "<GND"
- board text added: "r1"
